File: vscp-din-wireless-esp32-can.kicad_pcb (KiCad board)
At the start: 2 copper layers, 64.8 x 51 mm, 28 parts, among them J1 Conn_Left_I2C, J2 Conn_Right_Power, J3 Conn_01x06, J4 Conn_01x02, U1 ESP32-WROOM-32D, U2 MCP2517FD-xSL, U3 SN65HVD232, Y1 4MHz

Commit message: shrinked to fit encapsulationy
 Please enter the commit message for your changes. Lines starting
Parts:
- moved J2 8.93 mm to (159.4, 97.5)
- moved J1 8.90 mm to (129.1, 97.6)
- moved REF** 5.77 mm to (168.9, 80.9)
- moved R5 5.73 mm to (121.7, 72.0)
- moved C6 5.61 mm to (154.1, 77.7)
- moved R4 5.61 mm to (138.9, 82.8)
- moved R7 5.61 mm to (138.9, 78.5)
- moved R9 5.61 mm to (129.5, 90.9)
- moved Y1 5.61 mm to (153.9, 85.9)
- moved D2 5.61 mm to (137.1, 90.4)
- moved J3 5.61 mm to (117.7, 72.0)
- moved J4 5.61 mm to (125.7, 90.9)
- moved R6 5.61 mm to (163.3, 65.3)
- moved C1 5.61 mm to (135.8, 56.4)
- moved C2 5.61 mm to (130.3, 63.8)
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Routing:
- net VCC: track 239.2 -> 192.2 mm
- net Net-(D2-Pad1): track 51.4 -> 37.1 mm, vias 1 -> 0
- net Net-(D2-Pad2): track 40.8 -> 37.3 mm
- net /RXD: track 53.5 -> 54.3 mm
- net GND: vias 15 -> 21
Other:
- board size 64.8 x 51 mm -> 64.6 x 46 mm
- board text added: "VSCP DIN Wireless ESP32 CAN Rev B"
- board text removed: "VSCP DIN Wireless ESP32 CAN Rev A"

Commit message: Fixed some design errors
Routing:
- net Net-(U1-Pad30): track 1.33 -> 0.00 mm
- net Net-(U1-Pad31): track 1.25 -> 0.00 mm
- net /ledb: track 29.7 -> 28.7 mm
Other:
- net class Default removed

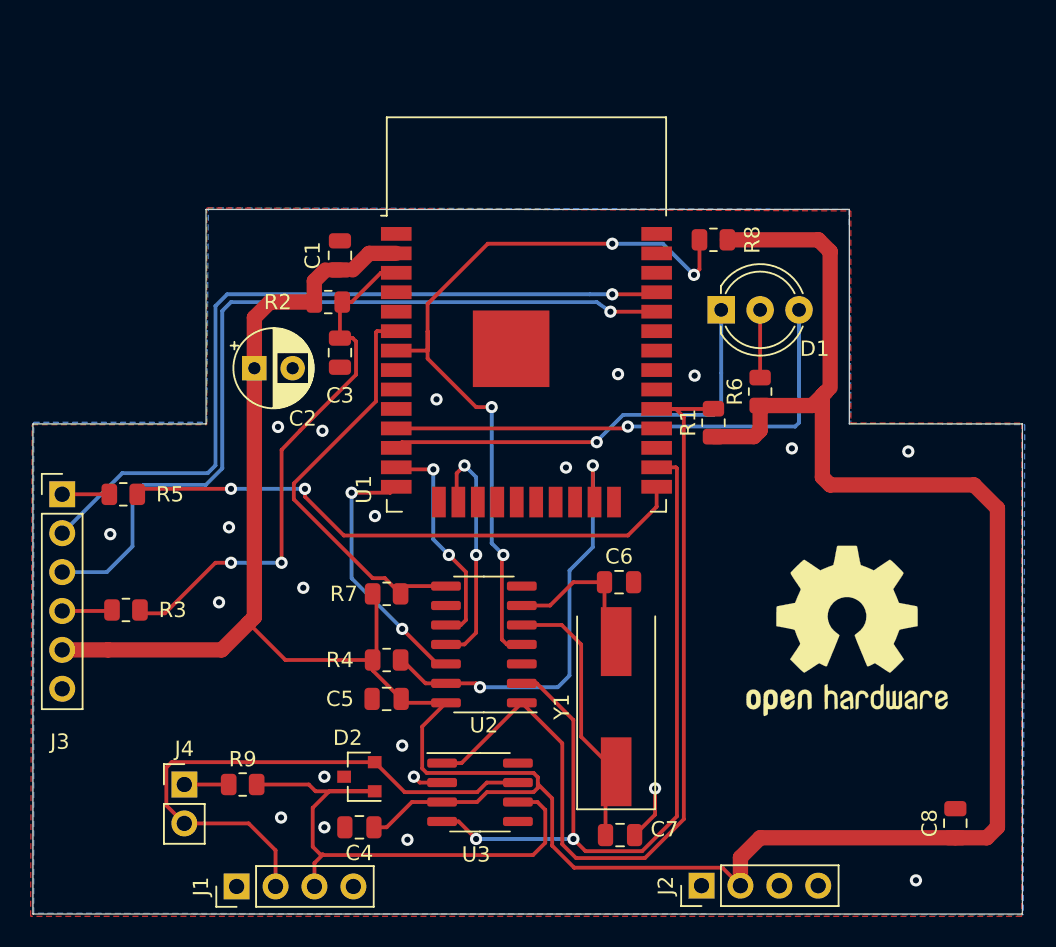
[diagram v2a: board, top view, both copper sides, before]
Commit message: Updated ESP32 module
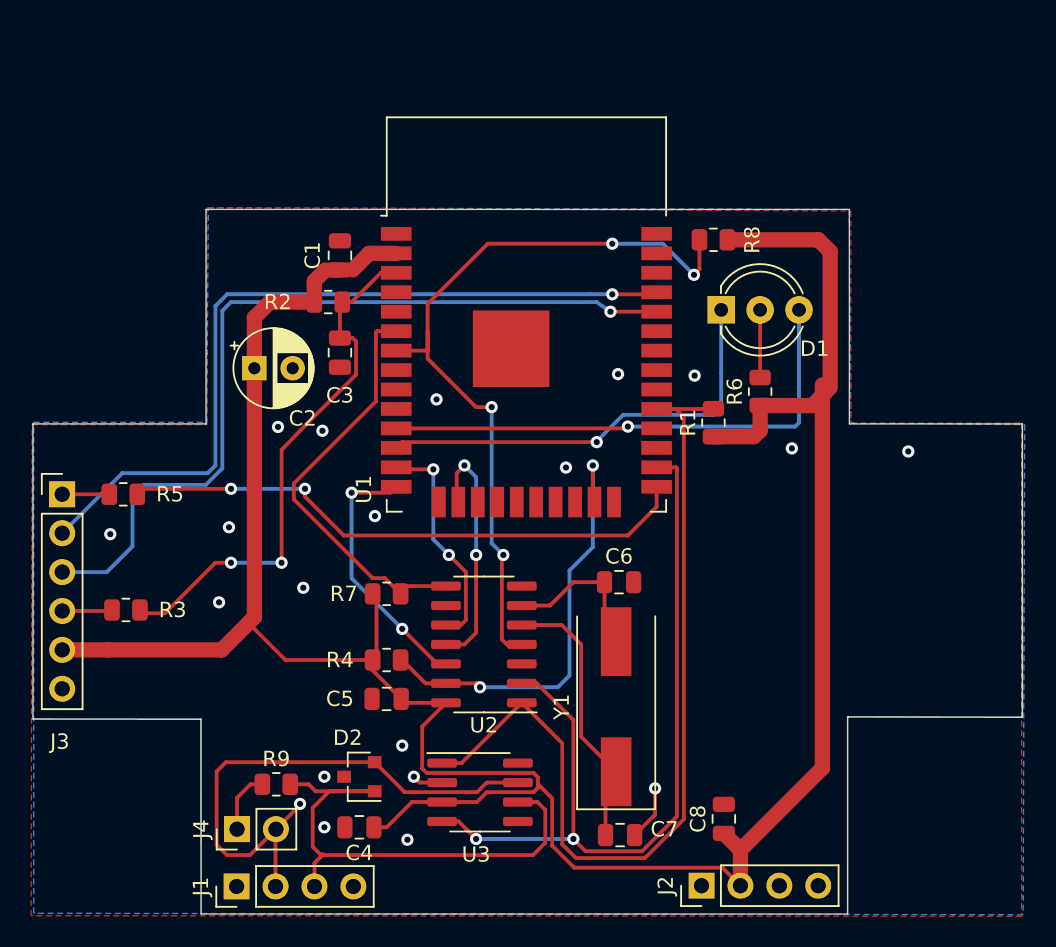
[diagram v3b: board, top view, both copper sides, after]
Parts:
- removed REF**: OSHW-Logo2_14.6x12mm_SilkScreen, Symbol:OSHW-Logo2_14.6x12mm_SilkScreen
- moved C8 15.1 mm to (160.9, 93.2)
- moved J4 4.51 mm to (129.1, 93.9), turned to 90 degrees
- moved R9 2.19 mm to (131.7, 90.9)
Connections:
- J1 pad 1: Net-(J1-Pad1) -> unconnected-(J1-Pin_1-Pad1)
- J2 pad 3: Net-(J2-Pad3) -> unconnected-(J2-Pin_3-Pad3)
- J2 pad 4: Net-(J2-Pad4) -> unconnected-(J2-Pin_4-Pad4)
- U1 pad 10: Net-(U1-Pad10) -> unconnected-(U1-IO25-Pad10)
- U1 pad 17: Net-(U1-Pad17) -> unconnected-(U1-SHD/SD2-Pad17)
- U1 pad 18: Net-(U1-Pad18) -> unconnected-(U1-SWP/SD3-Pad18)
- U1 pad 19: Net-(U1-Pad19) -> unconnected-(U1-SCS/CMD-Pad19)
- U1 pad 20: Net-(U1-Pad20) -> unconnected-(U1-SCK/CLK-Pad20)
- U1 pad 21: Net-(U1-Pad21) -> unconnected-(U1-SDO/SD0-Pad21)
- U1 pad 22: Net-(U1-Pad22) -> unconnected-(U1-SDI/SD1-Pad22)
- U1 pad 24: Net-(U1-Pad24) -> unconnected-(U1-IO2-Pad24)
- U1 pad 27: Net-(U1-Pad27) -> unconnected-(U1-IO16-Pad27)
- U1 pad 28: Net-(U1-Pad28) -> unconnected-(U1-IO17-Pad28)
- U1 pad 30: Net-(U1-Pad30) -> unconnected-(U1-IO18-Pad30)
- U1 pad 31: Net-(U1-Pad31) -> unconnected-(U1-IO19-Pad31)
- U1 pad 32: Net-(U1-Pad32) -> unconnected-(U1-NC-Pad32)
- U1 pad 33: Net-(U1-Pad33) -> unconnected-(U1-IO21-Pad33)
- U1 pad 36: Net-(U1-Pad36) -> unconnected-(U1-IO22-Pad36)
- U1 pad 37: Net-(U1-Pad37) -> unconnected-(U1-IO23-Pad37)
- U1 pad 4: Net-(U1-Pad4) -> unconnected-(U1-SENSOR_VP-Pad4)
- U1 pad 5: Net-(U1-Pad5) -> unconnected-(U1-SENSOR_VN-Pad5)
- U1 pad 8: Net-(U1-Pad8) -> unconnected-(U1-IO32-Pad8)
- U1 pad 9: Net-(U1-Pad9) -> unconnected-(U1-IO33-Pad9)
- U2 pad 3: Net-(U2-Pad3) -> unconnected-(U2-CLKO/SOF-Pad3)
- U2 pad 9: Net-(U2-Pad9) -> unconnected-(U2-~{INT0}/GPIO0/XSTBY-Pad9)
- U3 pad 5: Net-(U3-Pad5) -> unconnected-(U3-NC-Pad5)
- U3 pad 8: Net-(U3-Pad8) -> unconnected-(U3-NC-Pad8)
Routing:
- net VCC: track 192.2 -> 170.7 mm
- net Net-(J1-Pin_3): track 37.1 -> 34.9 mm
- net Net-(J4-Pin_1): track 2.90 -> 4.06 mm
- net Net-(J1-Pin_2): track 37.3 -> 36.7 mm, vias 0 -> 1
- net GND: vias 21 -> 19
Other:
- outline, holes or cut-outs redrawn
- board text added: "VSCP DIN Wireless ESP32 CAN Z105 Rev B"
- board text removed: "VSCP DIN Wireless ESP32 CAN Rev B"
